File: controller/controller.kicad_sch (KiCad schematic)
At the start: 19 parts, among them J1 USB_B, J2 Barrel_Jack_Switch, J3 Conn_01x02, P1 PMOD-Device-x2-Type-Generic-A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, P2 PMOD-Device-x2-Type-Generic-A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, P3 PMOD-Device-x2-Type-Generic-A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, U1 MAX4820xUP, U2 USB3300-EZK, U3 NUCLEO144-F767ZI, U4 TSR_1-2450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

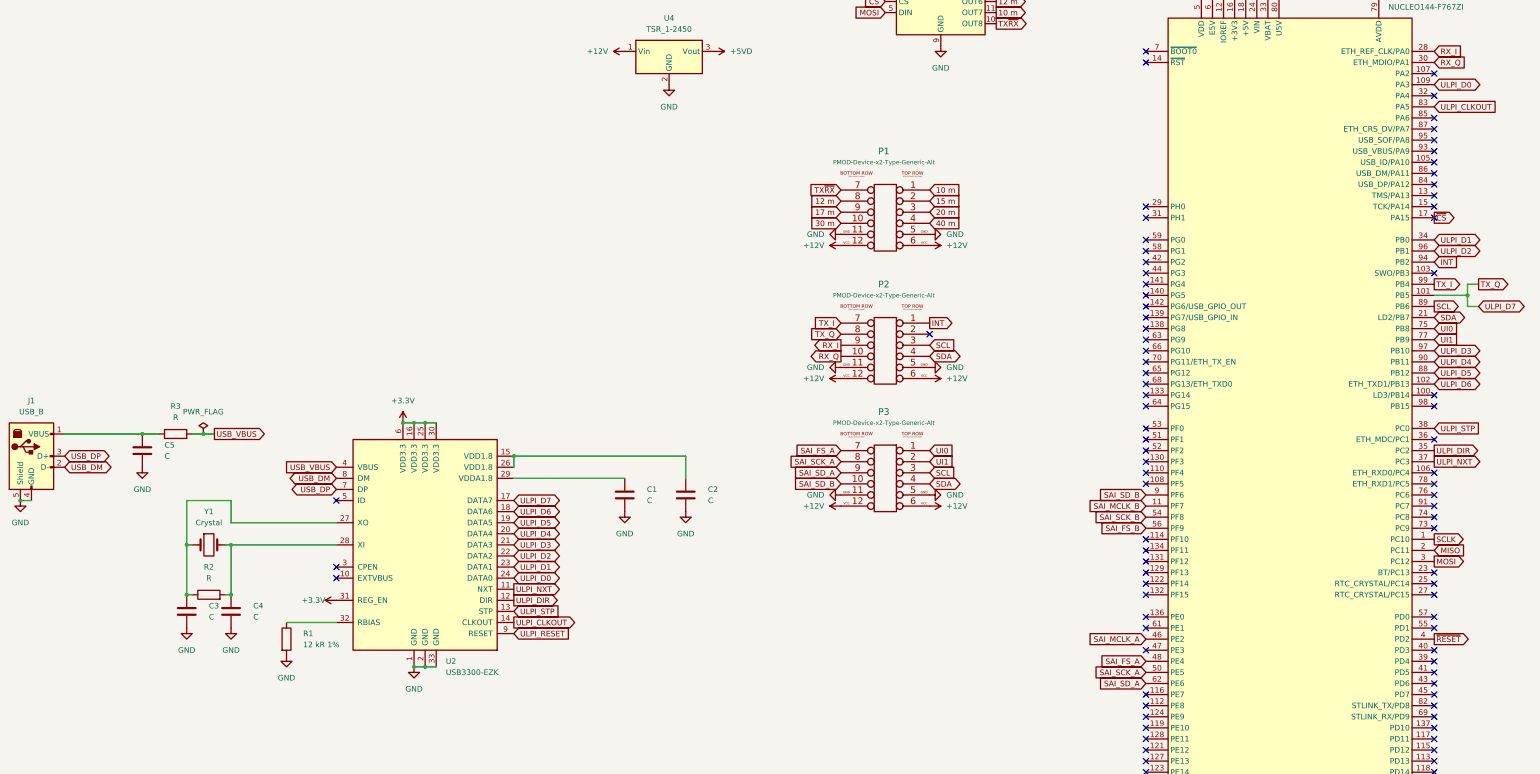
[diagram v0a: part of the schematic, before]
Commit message: remove USB HS PHY
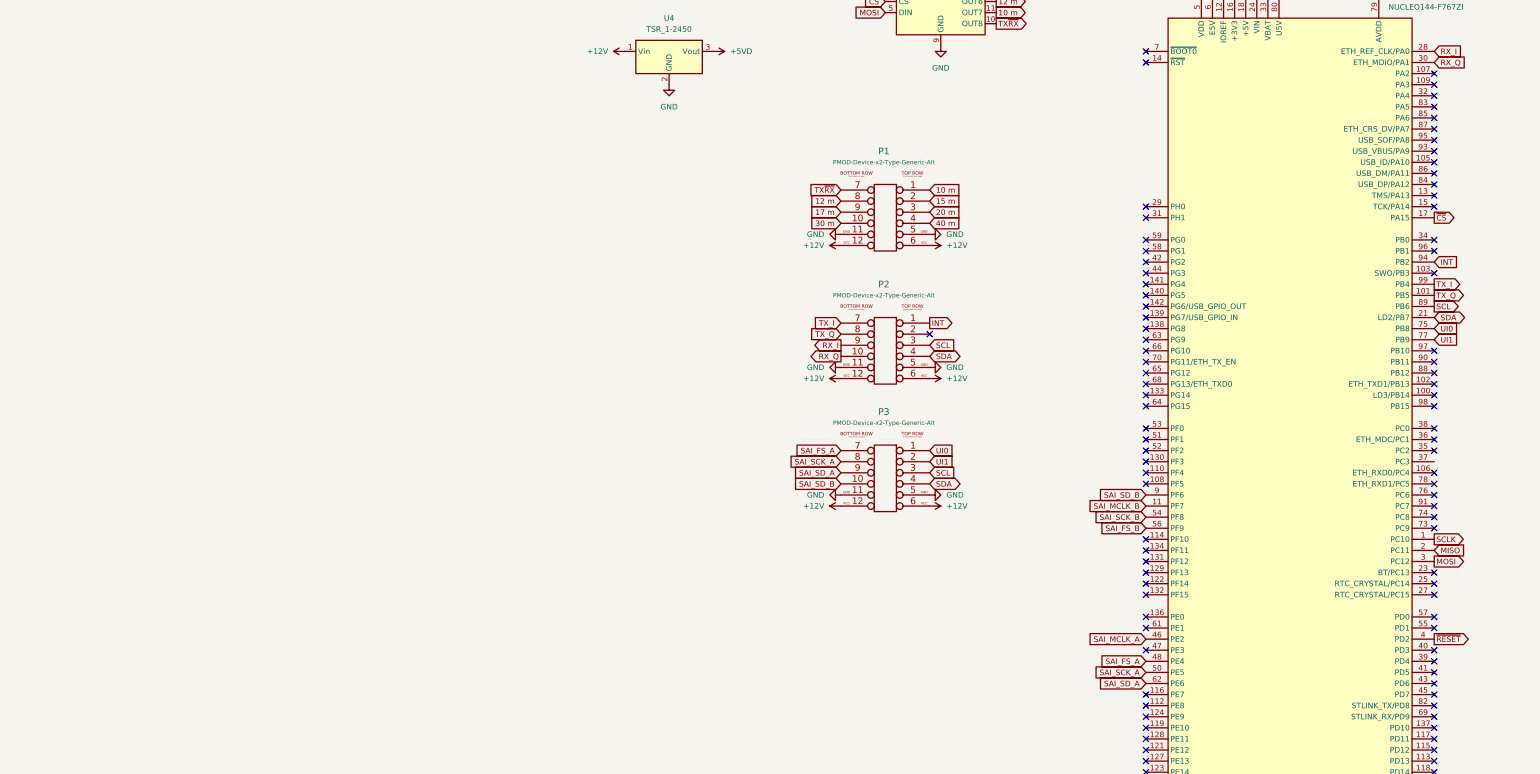
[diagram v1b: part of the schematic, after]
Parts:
- removed C1, C2, C5: C, symbol Device:C
- removed C3, C4: C, Capacitor_SMD:C_0603_1608Metric, symbol Device:C
- removed J1: USB_B, symbol Connector:USB_B
- removed R1: 12 kR 1%, Resistor_SMD:R_0603_1608Metric, symbol Device:R
- removed R2, R3: R, Resistor_SMD:R_0603_1608Metric, symbol Device:R
- removed U2: USB3300-EZK, Package_DFN_QFN:QFN-32-1EP_5x5mm_P0.5mm_EP3.45x3.45mm, symbol Interface_USB:USB3300-EZK
- removed Y1: Crystal, symbol Device:Crystal
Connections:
- net ULPI_CLKOUT: no longer names the net of U3.83 (PA5)
- net ULPI_D0: no longer names the net of U3.109 (PA3)
- net ULPI_D1: no longer names the net of U3.34 (PB0)
- net ULPI_D2: no longer names the net of U3.96 (PB1)
- net ULPI_D3: no longer names the net of U3.97 (PB10)
- net ULPI_D4: no longer names the net of U3.90 (PB11)
- net ULPI_D5: no longer names the net of U3.88 (PB12)
- net ULPI_D6: no longer names the net of U3.102 (ETH_TXD1/PB13)
- net ULPI_DIR: no longer names the net of U3.35 (PC2)
- net ULPI_NXT: no longer names the net of U3.37 (PC3)
- net ULPI_STP: no longer names the net of U3.38 (PC0)
- no-connect marks 96 -> 102

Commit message: clean up
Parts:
- U3: footprint Module:ST_Morpho_Connector_144_STLink -> pico-sdx:ST_Morpho_and_Zio_Connectors_144_STLink
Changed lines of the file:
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@@
 			)
 		)
-		(property "Footprint" "Module:ST_Morpho_Connector_144_STLink"
+		(property "Footprint" "pico-sdx:ST_Morpho_and_Zio_Connectors_144_STLink"
 			(at 152.4 236.22 0)
 			(effects

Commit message: use ZIO footprint for Nucleo
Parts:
- removed U1: MAX4820xUP, Package_SO:HTSSOP-20-1EP_4.4x6.5mm_P0.65mm_EP2.85x4mm, symbol Driver_Relay:MAX4820xUP
- removed U3: NUCLEO144-F767ZI, pico-sdx:ST_Morpho_and_Zio_Connectors_144_STLink, symbol MCU_Module:NUCLEO144-F767ZI
- removed U4: TSR_1-2450, Converter_DCDC:Converter_DCDC_TRACO_TSR-1_THT, symbol Regulator_Switching:TSR_1-2450
- added A1: NUCLEO144-H767ZI, crossover:ST_Zio_Connectors_144_STLink, symbol crossover:NUCLEO144-H767ZI
- added U3: ULN2803A, Package_SO:SOIC-18W_7.5x11.6mm_P1.27mm, symbol Transistor_Array:ULN2803A
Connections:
- net +12V: now also A1.CN8_15 (VIN), U3.10 (COM)
- net +3.3V: now also A1.CN8_7 (+3V3)
- net 10 m: now also U3.12 (O7)
- net 12 m: now also U3.13 (O6)
- net 15 m: now also U3.14 (O5)
- net 17 m: now also U3.15 (O4)
- net 20 m: now also U3.16 (O3)
- net 30 m: now also U3.17 (O2)
- net 40 m: now also U3.18 (O1)
- net GND: now also A1.CN10_17 (GND_CN10), A1.CN10_22 (GND_CN10), A1.CN10_27 (GND_CN10), A1.CN10_3 (AGND_CN10), A1.CN10_5 (GND_CN10), A1.CN7_8 (GND_CN7), A1.CN8_11 (GND_CN8), A1.CN8_13 (GND_CN8), A1.CN9_12 (GND_CN9), A1.CN9_23 (GND_CN9), U3.9 (GND)
- net INT: now also A1.CN7_7 (D19/PB12/I2S_A_WS)
- net RX_I: now also A1.CN10_7 (A6/PB1/ADC_A_IN)
- net RX_Q: now also A1.CN10_9 (A7/PC2/ADC_B_IN)
- net SAI_FS_A: now also A1.CN9_16 (D57/PE4/SAI_A_FS)
- net SAI_FS_B: now also A1.CN9_28 (D63/PF9/SAI_B_FS)
- net SAI_MCLK_A: now also A1.CN9_14 (D56/PE2/SAI_A_MCLK)
- net SAI_MCLK_B: now also A1.CN9_26 (D62/PF7/SAI_B_MCLK)
- net SAI_SCK_A: now also A1.CN9_18 (D58/PE5/SAI_A_SCK)
- net SAI_SCK_B: now also A1.CN9_24 (D61/PF8/SAI_B_SCK)
- net SAI_SD_A: now also A1.CN9_20 (D59/PE6/SAI_A_SD)
- net SAI_SD_B: now also A1.CN9_22 (D60/PE3/SAI_B_SD)
- net SCL: now also A1.CN7_2 (D15/PB8/I2C_A_SCL)
- net SDA: now also A1.CN7_4 (D14/PB9/I2C_A_SDA)
- net TX_I: now also A1.CN7_10 (D13/PA5/SPI_A_SCK)
- net TX_Q: now also A1.CN7_17 (D24/PA4/SPI_B_NSS)
- net TX~{RX}: now also U3.11 (O8)
- net UI0: now also A1.CN10_16 (D0/PG9/USART_A_RX)
- net UI1: now also A1.CN10_14 (D1/PG14/USART_A_TX)
- new net: A1.CN8_10 (D47/PC12/SDMMC_CK), U3.5 (I5)
- new net: A1.CN8_12 (D48/PD2/SDMMC_CMD), U3.6 (I6)
- new net: A1.CN8_14 (D49/PG2/IO), U3.7 (I7)
- new net: A1.CN8_16 (D50/PG3/IO), U3.8 (I8)
- new net: A1.CN8_2 (D43/PC8/SDMMC_D0), U3.1 (I1)
- new net: A1.CN8_4 (D44/PC9/SDMMC_D1/I2S_B_CKIN), U3.2 (I2)
- new net: A1.CN8_6 (D45/PC10/SDMMC_D2), U3.3 (I3)
- new net: A1.CN8_8 (D46/PC11/SDMMC_D3), U3.4 (I4)
- no-connect marks 102 -> 63

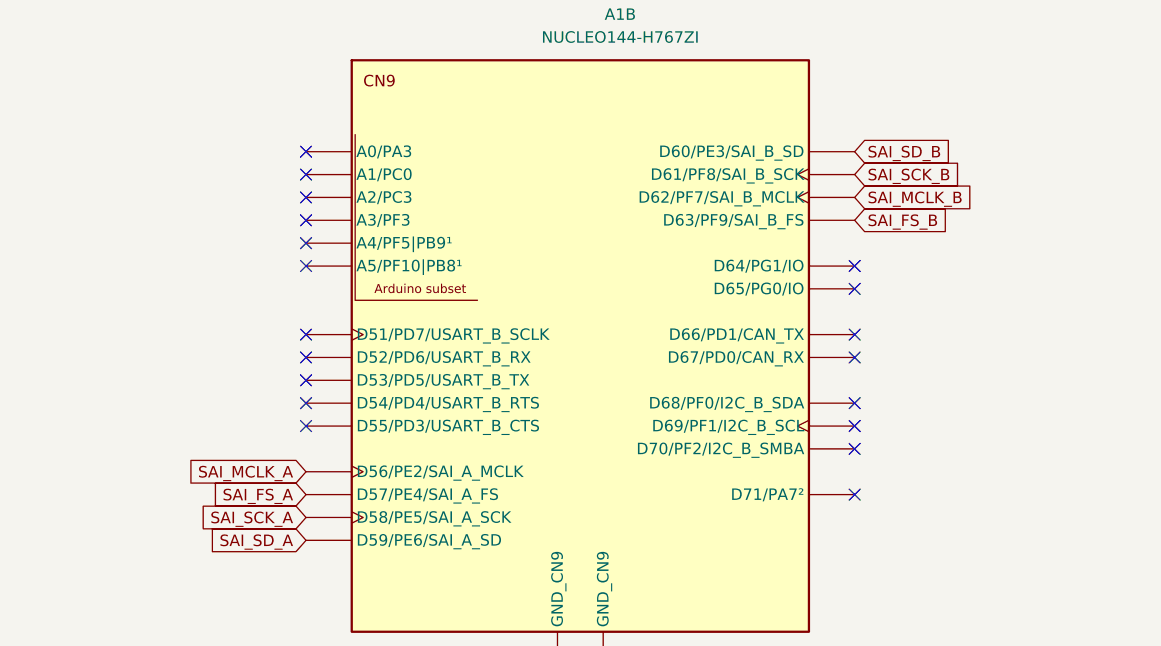
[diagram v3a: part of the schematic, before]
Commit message: remove external symbol and footprint libraries
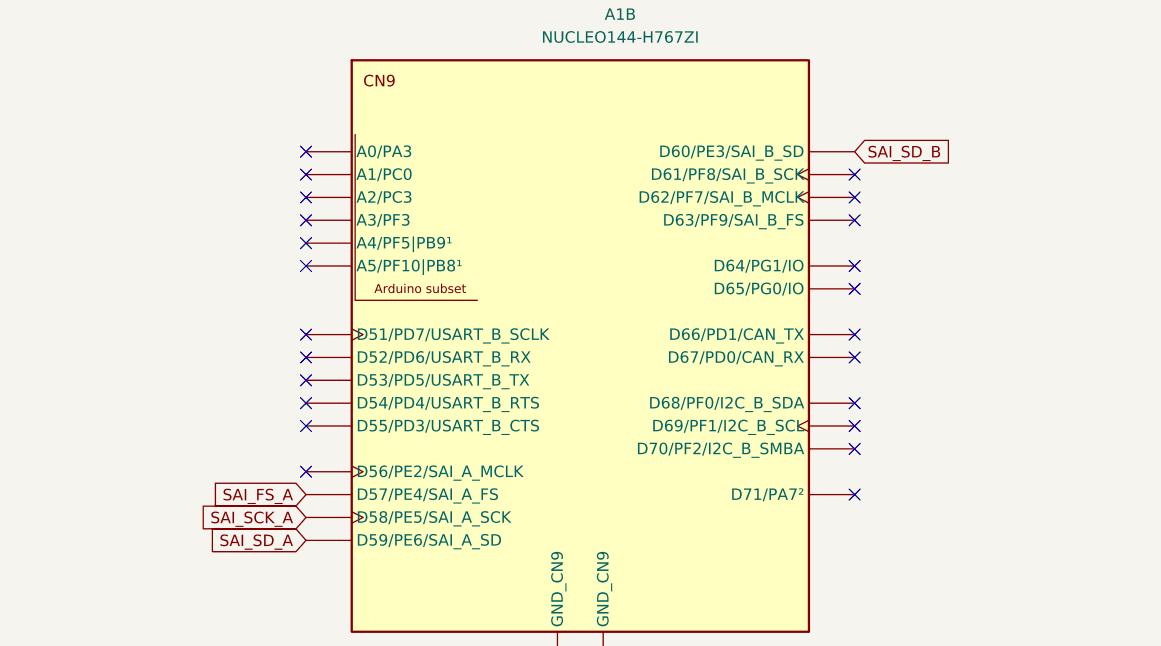
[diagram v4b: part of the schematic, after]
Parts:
- A1: footprint crossover:ST_Zio_Connectors_144_STLink -> pico-sdx:ST_Zio_Connectors_144_STLink; symbol crossover:NUCLEO144-H767ZI -> pico-sdx:NUCLEO144-H767ZI
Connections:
- net SAI_FS_B: no longer names the net of A1.CN9_28 (D63/PF9/SAI_B_FS)
- net SAI_MCLK_A: no longer names the net of A1.CN9_14 (D56/PE2/SAI_A_MCLK)
- net SAI_MCLK_B: no longer names the net of A1.CN9_26 (D62/PF7/SAI_B_MCLK)
- net SAI_SCK_B: no longer names the net of A1.CN9_24 (D61/PF8/SAI_B_SCK)
- no-connect marks 63 -> 67
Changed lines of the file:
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@@
 	)
 	(no_connect
+		(at -33.02 193.04)
+	)
+	(no_connect
 		(at 284.48 210.82)
 	)
@@
 	)
 	(no_connect
+		(at -93.98 223.52)
+	)
+	(no_connect
 		(at -93.98 190.5)
 	)
@@
 	)
 	(no_connect
+		(at -33.02 190.5)
+	)
+	(no_connect
 		(at 218.44 195.58)
 	)
@@
 	)
 	(no_connect
+		(at -33.02 195.58)
+	)
+	(no_connect
 		(at 218.44 238.76)
 	)
@@
 		)
 	)
-	(global_label "SAI_MCLK_B"
-		(shape input)
-		(at -33.02 193.04 0)
-		(fields_autoplaced yes)
-		(effects
-			(font
-				(size 1.27 1.27)
-			)
-			(justify left)
-		)
-		(property "Intersheetrefs" "${INTERSHEET_REFS}"
-			(at -18.9072 193.04 0)
-			(effects
-				(font
-					(size 1.27 1.27)
-				)
-				(justify left)
-				(hide yes)
-			)
-		)
-	)
 	(global_label "TX~{RX}"
 		(shape input)
@@
 		)
 	)
-	(global_label "SAI_SCK_B"
-		(shape input)
-		(at -33.02 190.5 0)
-		(fields_autoplaced yes)
-		(effects
-			(font
-				(size 1.27 1.27)
-			)
-			(justify left)
-		)
-		(property "Intersheetrefs" "${INTERSHEET_REFS}"
-			(at -20.1772 190.5 0)
-			(effects
-				(font
-					(size 1.27 1.27)
-				)
-				(justify left)
-				(hide yes)
-			)
-		)
-	)
 	(global_label "TX_I"
 		(shape output)
@@
 		)
 	)
-	(global_label "SAI_FS_B"
-		(shape input)
-		(at -33.02 195.58 0)
-		(fields_autoplaced yes)
-		(effects
-			(font
-				(size 1.27 1.27)
-			)
-			(justify left)
-		)
-		(property "Intersheetrefs" "${INTERSHEET_REFS}"
-			(at -21.6286 195.58 0)
-			(effects
-				(font
-					(size 1.27 1.27)
-				)
-				(justify left)
-				(hide yes)
-			)
-		)
-	)
 	(global_label "UI0"
 		(shape input)
@@
 		)
 	)
-	(global_label "SAI_MCLK_A"
-		(shape input)
-		(at -93.98 223.52 180)
-		(fields_autoplaced yes)
-		(effects
-			(font
-				(size 1.27 1.27)
-			)
-			(justify right)
-		)
-		(property "Intersheetrefs" "${INTERSHEET_REFS}"
-			(at -107.9114 223.52 0)
-			(effects
-				(font
-					(size 1.27 1.27)
-				)
-				(justify right)
-				(hide yes)
-			)
-		)
-	)
 	(global_label "15 m"
 		(shape input)
@@
 	)
 	(symbol
-		(lib_id "crossover:NUCLEO144-H767ZI")
+		(lib_id "pico-sdx:NUCLEO144-H767ZI")
 		(at 252.73 123.19 0)
 		(unit 3)
@@
 			)
 		)
-		(property "Footprint" "crossover:ST_Zio_Connectors_144_STLink"
+		(property "Footprint" "pico-sdx:ST_Zio_Connectors_144_STLink"
 			(at 252.73 52.07 0)
 			(effects
@@
 	)
 	(symbol
-		(lib_id "crossover:NUCLEO144-H767ZI")
+		(lib_id "pico-sdx:NUCLEO144-H767ZI")
 		(at -63.5 210.82 0)
 		(unit 2)
@@
 			)
 		)
-		(property "Footprint" "crossover:ST_Zio_Connectors_144_STLink"
+		(property "Footprint" "pico-sdx:ST_Zio_Connectors_144_STLink"
 			(at -63.5 139.7 0)
 			(effects
@@
 	)
 	(symbol
-		(lib_id "crossover:NUCLEO144-H767ZI")
+		(lib_id "pico-sdx:NUCLEO144-H767ZI")
 		(at -64.77 121.92 0)
 		(unit 1)
@@
 			)
 		)
-		(property "Footprint" "crossover:ST_Zio_Connectors_144_STLink"
+		(property "Footprint" "pico-sdx:ST_Zio_Connectors_144_STLink"
 			(at -64.77 50.8 0)
 			(effects
@@
 	)
 	(symbol
-		(lib_id "crossover:NUCLEO144-H767ZI")
+		(lib_id "pico-sdx:NUCLEO144-H767ZI")
 		(at 251.46 215.9 0)
 		(unit 4)
@@
 			)
 		)
-		(property "Footprint" "crossover:ST_Zio_Connectors_144_STLink"
+		(property "Footprint" "pico-sdx:ST_Zio_Connectors_144_STLink"
 			(at 251.46 144.78 0)
 			(effects
